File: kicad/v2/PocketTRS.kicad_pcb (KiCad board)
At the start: 2 copper layers, 87.6 x 73.9 mm, 44 parts, among them J1 TRS-80, J2 AudioJack3, J3 Mini-DIN-6, J4 DB15_Female_HighDensity, J5 Programmer, J6 USB_B_Micro, J7 PTRS_RESET, J8 ESP_RESET, Q1 BSS138, Q2 MMBT3904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

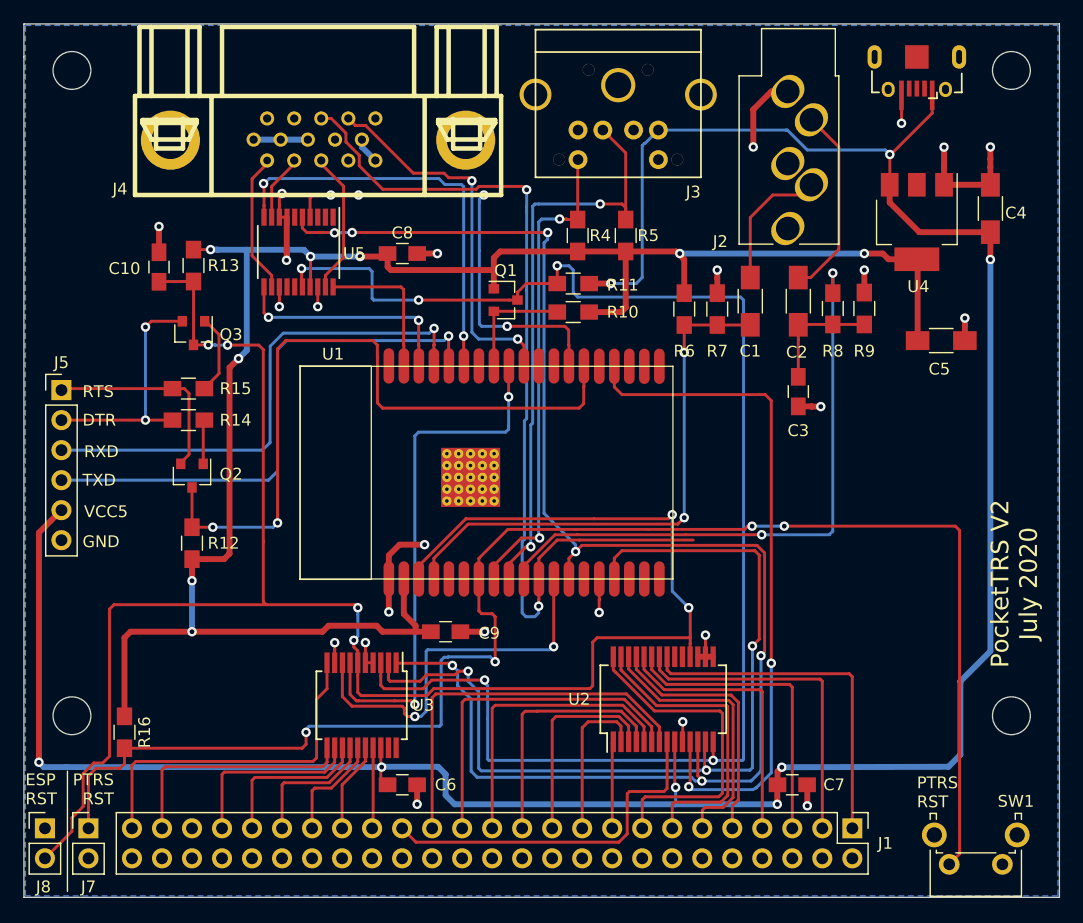
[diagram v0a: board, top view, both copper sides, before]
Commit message: Kicad V2 Fixes for PS/2 Keyboard
Changed PS2_DATA to GPIO32 and PS2_CLK to GPIO33
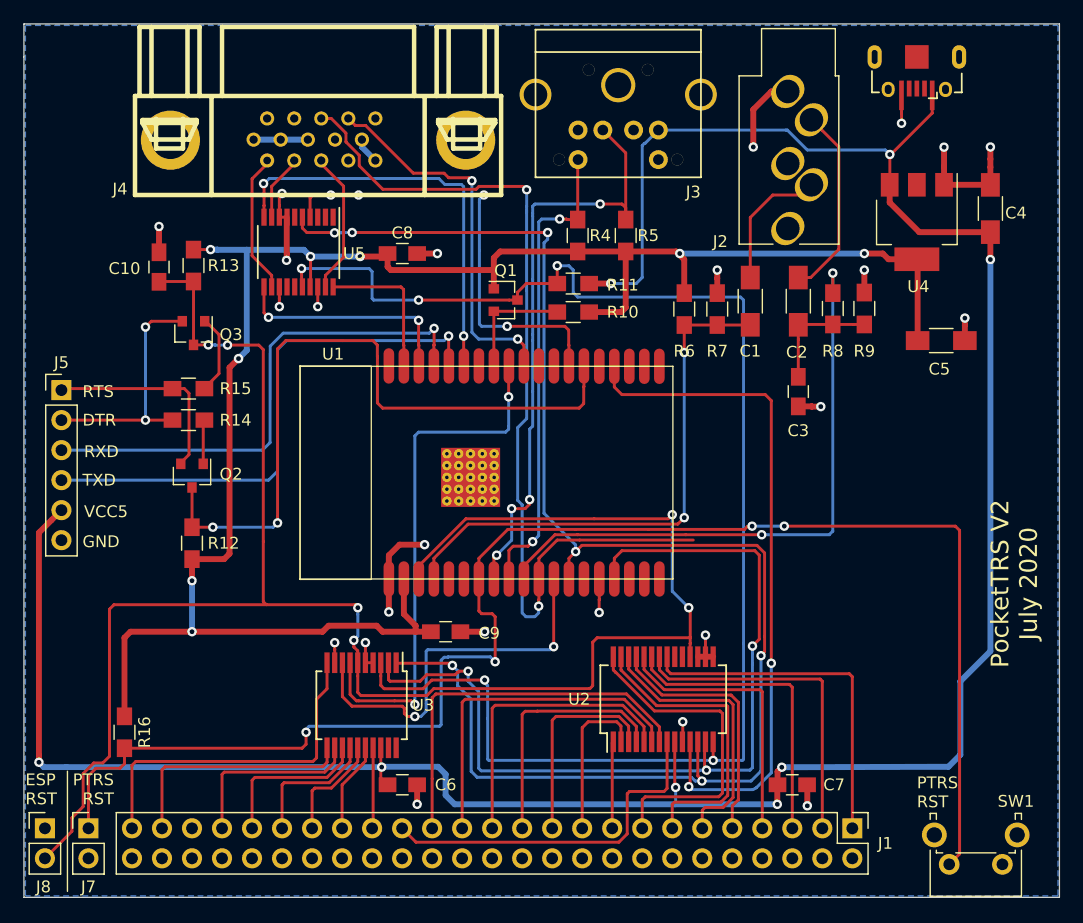
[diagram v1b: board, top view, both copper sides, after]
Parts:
- removed REF** (x4): MountingHole_3.2mm_M3, Mounting_Holes:MountingHole_3.2mm_M3
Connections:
- U1 pad 8: PS2_CLK -> PS2_DATA
- U1 pad 9: PS2_DATA -> PS2_CLK
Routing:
- net PS2_CLK: track 42.3 -> 40.5 mm
- net PS2_DATA: track 52.1 -> 51.0 mm, vias 2 -> 4
